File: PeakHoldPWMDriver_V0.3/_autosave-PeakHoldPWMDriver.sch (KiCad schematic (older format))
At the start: 120 parts, among them J1 RND 205-00203, J2 RND 205-00205, Q1 2N7002, Q10 2N7002, Q11 2N7002, Q12 2N7002, Q13 TSM2309, Q14 IRLL 024N, Q15 TSM2309, Q16 IRLL 024N, Q17 TSM2309, Q18 TSM2309, Q19 TSM2309, Q2 2N7002, Q20 TSM2309, Q3 2N7002, Q4 2N7002, Q5 TSM2309, Q6 TSM2309, Q7 IRLL 024N, Q8 IRLL 024N, Q9 2N7002, U1 74LS32, U2 LM2901, U3 74LS74, U4 LTC6992, U5 74LS74, U6 LM340, U7 74LS08, U8 74LS08, U9 LM2904

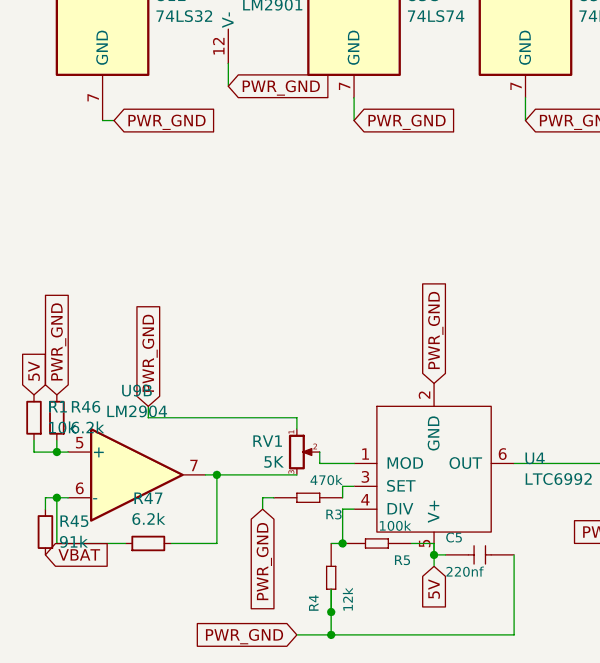
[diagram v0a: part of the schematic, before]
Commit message: PCB and schematic updated with battery voltage compensation
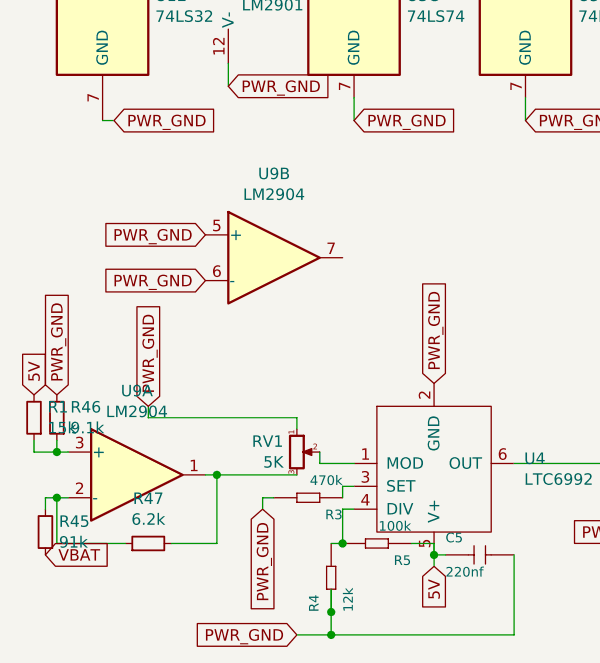
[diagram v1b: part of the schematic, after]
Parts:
- added unit 2 of U9
- R1: value 10k -> 15k
- R46: value 6.2k -> 9.1k
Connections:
- net PWR_GND: now also U9.5 (+), U9.6 (-)
- net at R47.2, RV1.3: now also U9.1; no longer U9.7
- net at R1.1, R46.1: now also U9.3 (+); no longer U9.5 (+)
- net at R45.2, R47.1: now also U9.2 (-); no longer U9.6 (-)
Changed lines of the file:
@@
 $Comp
 L Amplifier_Operational:LM2904 U9
-U 2 1 5F317FCB
+U 1 1 5F317FCB
 P 1000 6650
 F 0 "U9" H 1000 7017 50  0000 C CNN
@@
 F 2 "Package_SO:SO-8_3.9x4.9mm_P1.27mm" H 1000 6650 50  0001 C CNN
 F 3 "http://www.ti.com/lit/ds/symlink/lm358.pdf" H 1000 6650 50  0001 C CNN
-	2    1000 6650
+	1    1000 6650
 	1    0    0    -1
 $EndComp
@@
 P 550 6400
 F 0 "R1" H 491 6354 50  0000 R CNN
-F 1 "10k" H 491 6445 50  0000 R CNN
+F 1 "15k" H 491 6445 50  0000 R CNN
 F 2 "Resistor_SMD:R_0603_1608Metric" H 550 6400 50  0001 C CNN
 F 3 "~" H 550 6400 50  0001 C CNN
@@
 P 650 6400
 F 0 "R46" H 591 6354 50  0000 R CNN
-F 1 "6.2k" H 591 6445 50  0000 R CNN
+F 1 "9.1k" H 591 6445 50  0000 R CNN
 F 2 "Resistor_SMD:R_0603_1608Metric" H 650 6400 50  0001 C CNN
 F 3 "~" H 650 6400 50  0001 C CNN
@@
 Wire Wire Line
 	650  6550 700  6550
+$Comp
+L Amplifier_Operational:LM2904 U9
+U 2 1 5F7AED14
+P 1600 5700
+F 0 "U9" H 1600 6067 50  0000 C CNN
+F 1 "LM2904" H 1600 5976 50  0000 C CNN
+F 2 "Package_SO:SO-8_3.9x4.9mm_P1.27mm" H 1600 5700 50  0001 C CNN
+F 3 "http://www.ti.com/lit/ds/symlink/lm358.pdf" H 1600 5700 50  0001 C CNN
+	2    1600 5700
+	1    0    0    -1
+$EndComp
+Text GLabel 1300 5600 0    50   Input ~ 0
+PWR_GND
+Text GLabel 1300 5800 0    50   Input ~ 0
+PWR_GND
 $EndSCHEMATC
